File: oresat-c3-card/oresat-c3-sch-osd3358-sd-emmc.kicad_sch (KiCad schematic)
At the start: 48 parts, among them J5 DM3BT-DSF-PEJS, U1 OSD3358-1G-ISM, U8 TCAN330, U9 SFEM016GB1EA1TO-I-GE-121-STD

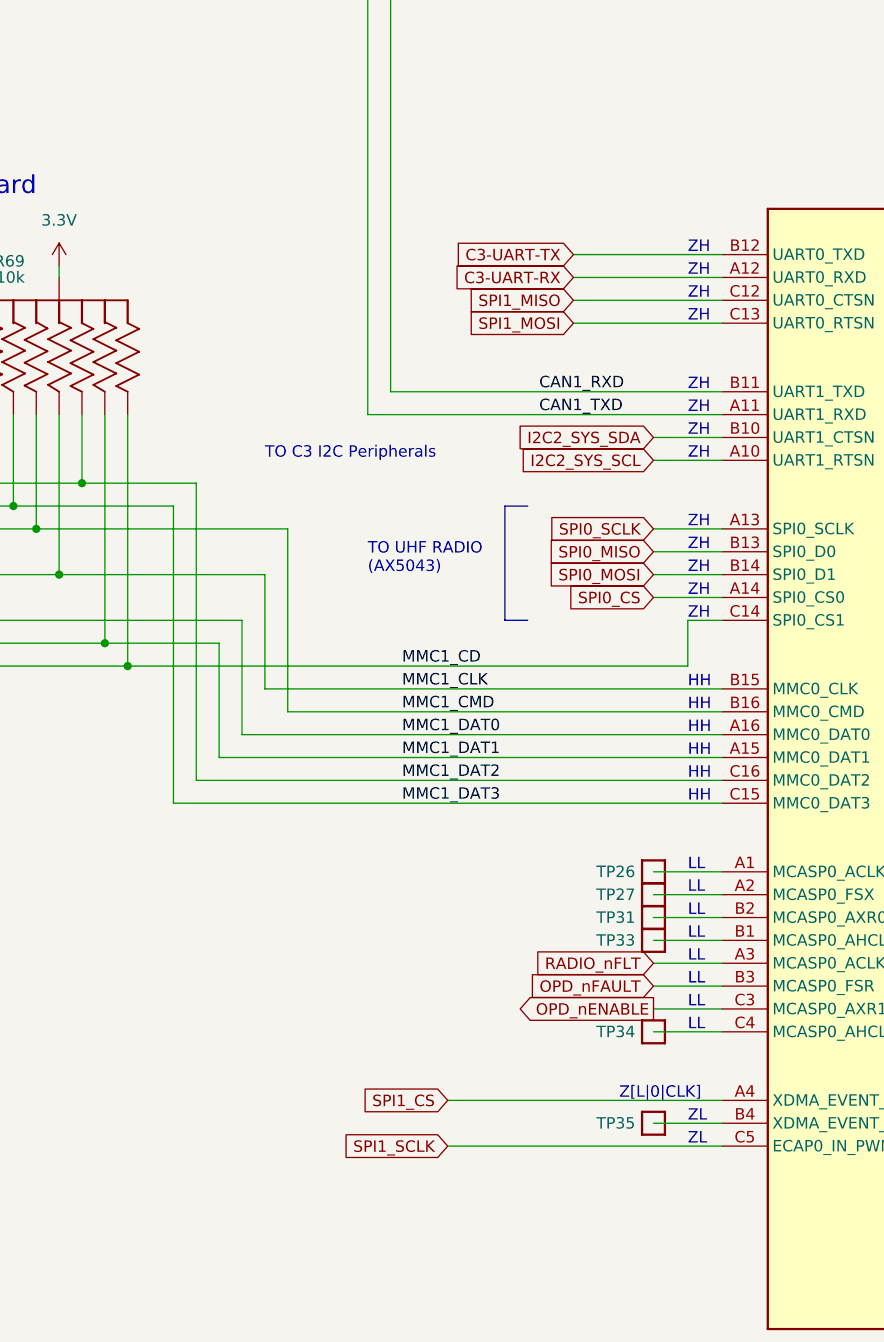
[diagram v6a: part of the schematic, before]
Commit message: Design review on C3 v7.0
Glenn and Andrew did a design review. Removed fiducials on back of board. Lots of schematic fixes, including
direction connection of TCXOs to AT86s, corrected LPF of CLKO from AT86 to the synth reference, fixed drive
levels both QPC switches in UHF radio, confirmed QPC directions, and some minor polishing.
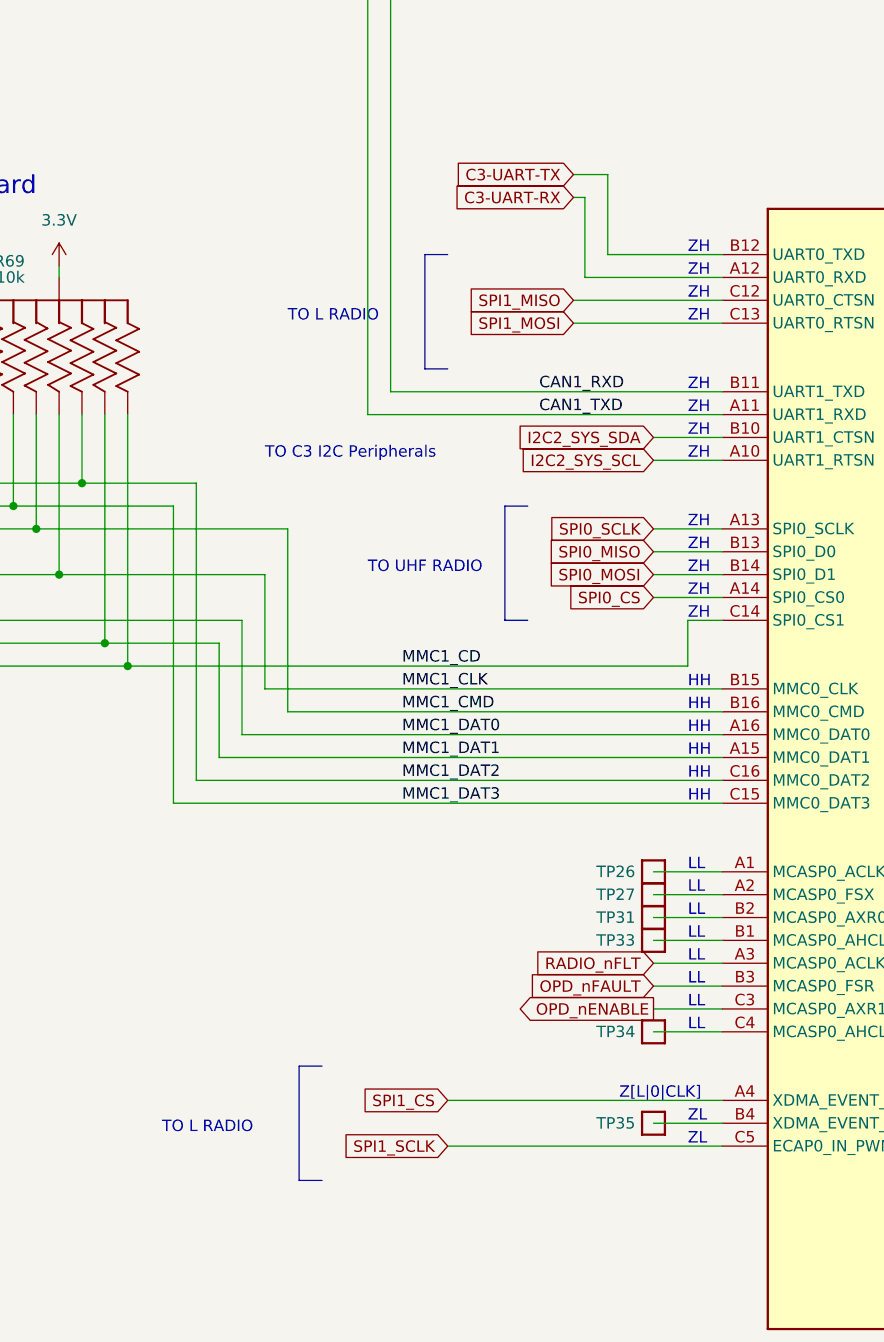
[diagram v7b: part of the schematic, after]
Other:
- note added: "TO L RADIO"
- note added: "TO UHF RADIO"
- note removed: "TO UHF RADIO (AX5043)"
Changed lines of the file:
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@@
 		)
 	)
+	(text "TO L RADIO"
+		(exclude_from_sim no)
+		(at 114.3 109.22 0)
+		(effects
+			(font
+				(size 1.27 1.27)
+			)
+			(justify left bottom)
+		)
+	)
 	(text "LL"
 		(exclude_from_sim no)
@@
 		)
 	)
+	(text "TO L RADIO"
+		(exclude_from_sim no)
+		(at 100.33 199.39 0)
+		(effects
+			(font
+				(size 1.27 1.27)
+			)
+			(justify left bottom)
+		)
+	)
 	(text "LL"
 		(exclude_from_sim no)
@@
 		)
 	)
-	(text "TO UHF RADIO\n(AX5043)"
+	(text "TO UHF RADIO"
 		(exclude_from_sim no)
 		(at 123.19 137.16 0)
@@
 	(wire
 		(pts
+			(xy 149.86 92.71) (xy 149.86 101.6)
+		)
+		(stroke
+			(width 0)
+			(type default)
+		)
+	)
+	(wire
+		(pts
 			(xy 281.94 154.94) (xy 281.94 165.1)
 		)
@@
 	(wire
 		(pts
+			(xy 147.32 104.14) (xy 162.56 104.14)
+		)
+		(stroke
+			(width 0)
+			(type default)
+		)
+	)
+	(wire
+		(pts
 			(xy 162.56 132.08) (xy 154.94 132.08)
 		)
@@
 		)
 	)
+	(polyline
+		(pts
+			(xy 132.08 101.6) (xy 129.54 101.6)
+		)
+		(stroke
+			(width 0)
+			(type default)
+		)
+	)
 	(wire
 		(pts
@@
 	(wire
 		(pts
+			(xy 147.32 95.25) (xy 147.32 104.14)
+		)
+		(stroke
+			(width 0)
+			(type default)
+		)
+	)
+	(wire
+		(pts
 			(xy 375.92 146.05) (xy 375.92 147.32)
 		)
@@
 	(wire
 		(pts
-			(xy 146.05 104.14) (xy 162.56 104.14)
+			(xy 146.05 95.25) (xy 147.32 95.25)
 		)
 		(stroke
@@
 		)
 	)
+	(polyline
+		(pts
+			(xy 129.54 101.6) (xy 129.54 114.3)
+		)
+		(stroke
+			(width 0)
+			(type default)
+		)
+	)
 	(wire
 		(pts
@@
 		)
 	)
+	(polyline
+		(pts
+			(xy 118.11 191.77) (xy 115.57 191.77)
+		)
+		(stroke
+			(width 0)
+			(type default)
+		)
+	)
 	(wire
 		(pts
@@
 		)
 	)
+	(polyline
+		(pts
+			(xy 115.57 204.47) (xy 118.11 204.47)
+		)
+		(stroke
+			(width 0)
+			(type default)
+		)
+	)
 	(wire
 		(pts
@@
 		)
 	)
+	(polyline
+		(pts
+			(xy 129.54 114.3) (xy 132.08 114.3)
+		)
+		(stroke
+			(width 0)
+			(type default)
+		)
+	)
 	(wire
 		(pts
@@
 	(wire
 		(pts
+			(xy 149.86 101.6) (xy 162.56 101.6)
+		)
+		(stroke
+			(width 0)
+			(type default)
+		)
+	)
+	(wire
+		(pts
 			(xy 345.44 152.4) (xy 345.44 153.67)
 		)
@@
 	(wire
 		(pts
-			(xy 146.05 101.6) (xy 162.56 101.6)
+			(xy 146.05 92.71) (xy 149.86 92.71)
 		)
 		(stroke
@@
 		)
 	)
+	(polyline
+		(pts
+			(xy 115.57 191.77) (xy 115.57 204.47)
+		)
+		(stroke
+			(width 0)
+			(type default)
+		)
+	)
 	(wire
 		(pts
@@
 	(global_label "C3-UART-RX"
 		(shape input)
-		(at 146.05 104.14 180)
+		(at 146.05 95.25 180)
 		(effects
 			(font
@@
 		)
 		(property "Intersheetrefs" "${INTERSHEET_REFS}"
-			(at 132.08 104.14 0)
+			(at 132.08 95.25 0)
 			(effects
 				(font
@@
 	(global_label "C3-UART-TX"
 		(shape input)
-		(at 146.05 101.6 180)
+		(at 146.05 92.71 180)
 		(effects
 			(font
@@
 		)
 		(property "Intersheetrefs" "${INTERSHEET_REFS}"
-			(at 131.826 101.6 0)
+			(at 131.826 92.71 0)
 			(effects
 				(font

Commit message: Updating BOM and switching to oresat-passive footprints. Fixed some power cutoff limits, and fixed another DC voltage leverl on an LNA!
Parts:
- C17, C18, C19, C20, C21, C22, C23, C24, D4, D5, D6, D7, J5, R69, R70, R71, U1, U8: DST Digi-Key -> DigiKey
- R42, R43, R44, R45: footprint Resistor_SMD:R_0603_1608Metric -> oresat-passives:0603-C-NOSILK; DST Digi-Key -> DigiKey; MFR Stackpole Electronics Inc -> Stackpole Electronics
- U9: DPN 1052-SFEM016GB1EA1TO-I-GE-121-STD-ND -> 3052-FDMM032GBE-3101-ND; DST Digi-Key -> DigiKey; MFR Swissbit -> Flexxon Pte Ltd; MPN SFEM016GB1EA1TO-I-GE-121-STD -> FDMM032GBE-3101
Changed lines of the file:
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@@
 			)
 		)
-		(property "Datasheet" "~"
+		(property "Datasheet" "https://www.we-online.com/components/products/datasheet/150060BS75000.pdf"
 			(at 293.37 104.14 90)
 			(effects
@@
 			)
 		)
-		(property "Description" "Light emitting diode, small symbol"
+		(property "Description" "Blue 470nm LED Indication - Discrete 3.2V 0603 (1608 Metric)"
 			(at 293.37 104.14 0)
 			(effects
@@
 			)
 		)
-		(property "DST" "Digi-Key"
+		(property "DST" "DigiKey"
 			(at 293.37 104.14 0)
 			(effects
@@
 			)
 		)
-		(property "Footprint" "Resistor_SMD:R_0603_1608Metric"
+		(property "Footprint" "oresat-passives:0603-C-NOSILK"
 			(at 280.67 119.38 0)
 			(effects
@@
 			)
 		)
-		(property "Datasheet" "~"
+		(property "Datasheet" "https://www.seielect.com/catalog/SEI-RMCF_RMCP.pdf"
 			(at 280.67 119.38 0)
 			(effects
@@
 			)
 		)
-		(property "DST" "Digi-Key"
+		(property "DST" "DigiKey"
 			(at 280.67 119.38 0)
 			(effects
@@
 			)
 		)
-		(property "MFR" "Stackpole Electronics Inc"
+		(property "MFR" "Stackpole Electronics"
 			(at 280.67 119.38 0)
 			(effects
@@
 			)
 		)
-		(property "DST" "Digi-Key"
+		(property "DST" "DigiKey"
 			(at 360.68 149.86 0)
 			(effects
@@
 			)
 		)
-		(property "DST" "Digi-Key"
+		(property "DST" "DigiKey"
 			(at 383.54 149.86 0)
 			(effects
@@
 			)
 		)
-		(property "Datasheet" "https://www.swissbit.com/data/EM-20/EM-20_fact_sheet.pdf"
+		(property "Datasheet" "https://www.flexxon.com/wp-content/uploads/Flexxon%20Profile/Flexxon-Brochure-Jan2020_compressed.pdf"
 			(at 330.2 175.26 0)
 			(effects
@@
 			)
 		)
-		(property "Description" "IC FLASH 16GBIT EMMC 153FBGA"
+		(property "Description" "Memory Card microSD™ 32GB UHS Class 1 TLC"
 			(at 330.2 175.26 0)
 			(effects
@@
 			)
 		)
-		(property "DPN" "1052-SFEM016GB1EA1TO-I-GE-121-STD-ND"
+		(property "DPN" "3052-FDMM032GBE-3101-ND"
 			(at 330.2 175.26 0)
 			(effects
@@
 			)
 		)
-		(property "DST" "Digi-Key"
+		(property "DST" "DigiKey"
 			(at 330.2 175.26 0)
 			(effects
@@
 			)
 		)
-		(property "MFR" "Swissbit"
+		(property "MFR" "Flexxon Pte Ltd"
 			(at 330.2 175.26 0)
 			(effects
@@
 			)
 		)
-		(property "MPN" "SFEM016GB1EA1TO-I-GE-121-STD"
+		(property "MPN" "FDMM032GBE-3101"
 			(at 330.2 175.26 0)
 			(effects
@@
 			)
 		)
-		(property "Footprint" "Resistor_SMD:R_0603_1608Metric"
+		(property "Footprint" "oresat-passives:0603-C-NOSILK"
 			(at 280.67 104.14 0)
 			(effects
@@
 			)
 		)
-		(property "Datasheet" "~"
+		(property "Datasheet" "https://www.seielect.com/catalog/SEI-RMCF_RMCP.pdf"
 			(at 280.67 104.14 0)
 			(effects
@@
 			)
 		)
-		(property "DST" "Digi-Key"
+		(property "DST" "DigiKey"
 			(at 280.67 104.14 0)
 			(effects
@@
 			)
 		)
-		(property "MFR" "Stackpole Electronics Inc"
+		(property "MFR" "Stackpole Electronics"
 			(at 280.67 104.14 0)
 			(effects
@@
 			)
 		)
-		(property "DST" "Digi-Key"
+		(property "DST" "DigiKey"
 			(at 191.77 63.5 0)
 			(effects
@@
 			)
 		)
-		(property "DST" "Digi-Key"
+		(property "DST" "DigiKey"
 			(at 368.3 149.86 0)
 			(effects
@@
 			)
 		)
-		(property "DST" "Digi-Key"
+		(property "DST" "DigiKey"
 			(at 345.44 149.86 0)
 			(effects
@@
 			)
 		)
-		(property "Datasheet" "~"
+		(property "Datasheet" "https://www.we-online.com/components/products/datasheet/150060BS75000.pdf"
 			(at 293.37 111.76 90)
 			(effects
@@
 			)
 		)
-		(property "Description" "Light emitting diode, small symbol"
+		(property "Description" "Blue 470nm LED Indication - Discrete 3.2V 0603 (1608 Metric)"
 			(at 293.37 111.76 0)
 			(effects
@@
 			)
 		)
-		(property "DST" "Digi-Key"
+		(property "DST" "DigiKey"
 			(at 293.37 111.76 0)
 			(effects
@@
 			)
 		)
-		(property "Datasheet" ""
+		(property "Datasheet" "https://octavosystems.com/docs/osd335x-sm-datasheet/"
 			(at 193.04 157.48 0)
 			(effects
@@
 			)
 		)
-		(property "DST" "Digi-Key"
+		(property "DST" "DigiKey"
 			(at 193.04 157.48 0)
 			(effects
@@
 			)
 		)
-		(property "DST" "Digi-Key"
+		(property "DST" "DigiKey"
 			(at 176.53 48.26 0)
 			(effects
@@
 			)
 		)
-		(property "Footprint" "Resistor_SMD:R_0603_1608Metric"
+		(property "Footprint" "oresat-passives:0603-C-NOSILK"
 			(at 280.67 111.76 0)
 			(effects
@@
 			)
 		)
-		(property "Datasheet" "~"
+		(property "Datasheet" "https://www.seielect.com/catalog/SEI-RMCF_RMCP.pdf"
 			(at 280.67 111.76 0)
 			(effects
@@
 			)
 		)
-		(property "DST" "Digi-Key"
+		(property "DST" "DigiKey"
 			(at 280.67 111.76 0)
 			(effects
@@
 			)
 		)
-		(property "MFR" "Stackpole Electronics Inc"
+		(property "MFR" "Stackpole Electronics"
 			(at 280.67 111.76 0)
 			(effects
@@
 			)
 		)
-		(property "Datasheet" "~"
+		(property "Datasheet" "https://www.we-online.com/components/products/datasheet/150060BS75000.pdf"
 			(at 293.37 119.38 90)
 			(effects
@@
 			)
 		)
-		(property "Description" "Light emitting diode, small symbol"
+		(property "Description" "Blue 470nm LED Indication - Discrete 3.2V 0603 (1608 Metric)"
 			(at 293.37 119.38 0)
 			(effects
@@
 			)
 		)
-		(property "DST" "Digi-Key"
+		(property "DST" "DigiKey"
 			(at 293.37 119.38 0)
 			(effects
@@
 			)
 		)
-		(property "DST" "Digi-Key"
+		(property "DST" "DigiKey"
 			(at 375.92 149.86 0)
 			(effects
@@
 			)
 		)
-		(property "DST" "Digi-Key"
+		(property "DST" "DigiKey"
 			(at 58.42 137.16 0)
 			(effects
@@
 			)
 		)
-		(property "DST" "Digi-Key"
+		(property "DST" "DigiKey"
 			(at 355.6 149.86 0)
 			(effects
@@
 			)
 		)
-		(property "Datasheet" "~"
+		(property "Datasheet" "https://www.we-online.com/components/products/datasheet/150060BS75000.pdf"
 			(at 293.37 127 90)
 			(effects
@@
 			)
 		)
-		(property "Description" "Light emitting diode, small symbol"
+		(property "Description" "Blue 470nm LED Indication - Discrete 3.2V 0603 (1608 Metric)"
 			(at 293.37 127 0)
 			(effects
@@
 			)
 		)
-		(property "DST" "Digi-Key"
+		(property "DST" "DigiKey"
 			(at 293.37 127 0)
 			(effects
@@
 			)
 		)
-		(property "DST" "Digi-Key"
+		(property "DST" "DigiKey"
 			(at 78.74 106.68 0)
 			(effects
@@
 			)
 		)
-		(property "Footprint" "Resistor_SMD:R_0603_1608Metric"
+		(property "Footprint" "oresat-passives:0603-C-NOSILK"
 			(at 280.67 127 0)
 			(effects
@@
 			)
 		)
-		(property "Datasheet" "~"
+		(property "Datasheet" "https://www.seielect.com/catalog/SEI-RMCF_RMCP.pdf"
 			(at 280.67 127 0)
 			(effects
@@
 			)
 		)
-		(property "DST" "Digi-Key"
+		(property "DST" "DigiKey"
 			(at 280.67 127 0)
 			(effects
@@
 			)
 		)
-		(property "MFR" "Stackpole Electronics Inc"
+		(property "MFR" "Stackpole Electronics"
 			(at 280.67 127 0)
 			(effects
@@
 			)
 		)
-		(property "DST" "Digi-Key"
+		(property "DST" "DigiKey"
 			(at 67.31 110.49 0)
 			(effects
@@
 			)
 		)
-		(property "DST" "Digi-Key"
+		(property "DST" "DigiKey"
 			(at 261.62 142.24 0)
 			(effects
@@
 			)
 		)
-		(property "DST" "Digi-Key"
+		(property "DST" "DigiKey"
 			(at 281.94 142.24 0)
 			(effects
